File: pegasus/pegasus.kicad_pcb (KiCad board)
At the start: 2 copper layers, 50 x 120 mm, 15 parts, among them IC1 RFD900, IC2 Adafruit_MPL3115A2, IC3 Adafruit-BNO055-PCB, IC4 L70B-M39, IC5 L7805ACV, J1 Conn_01x02_Female, J2 Conn_01x02_Female, U1 Teensy4.1, U2 CON-SMA-EDGE-S, U3 CON-SMA-EDGE-S

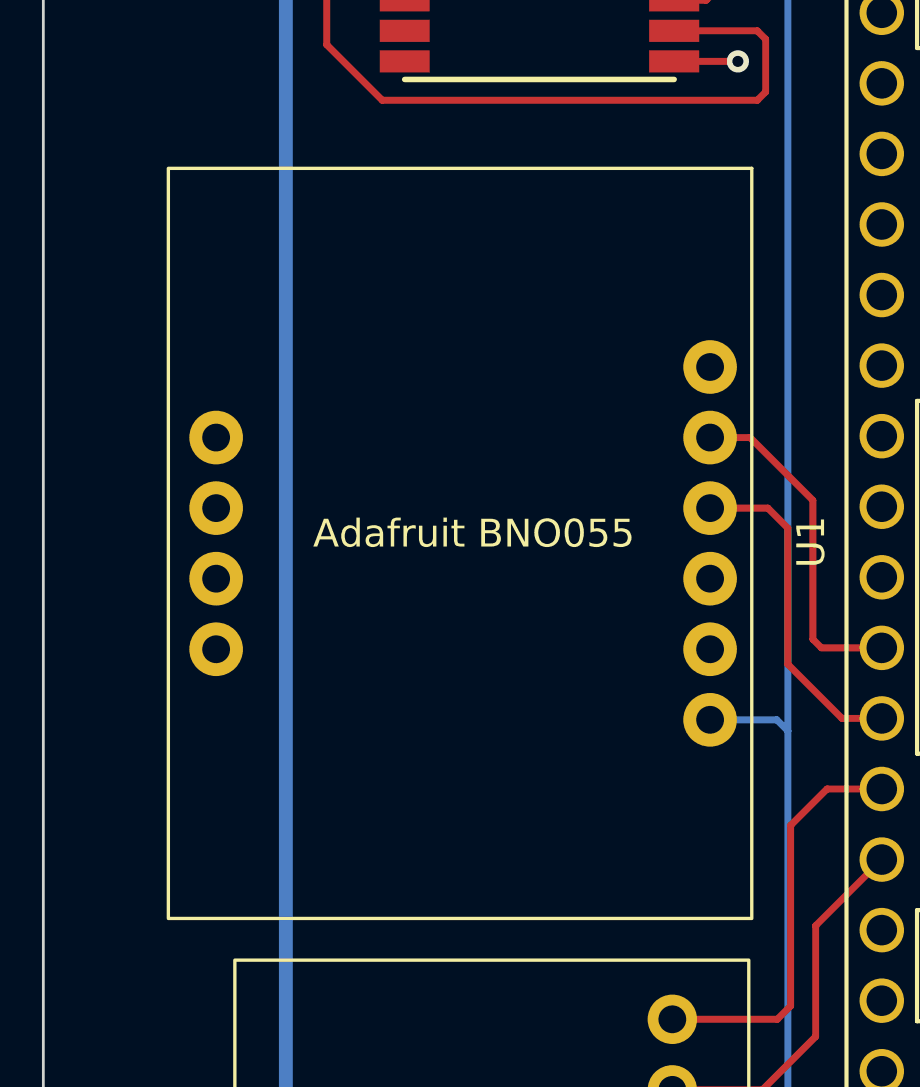
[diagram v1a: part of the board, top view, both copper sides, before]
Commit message: improved dimensional accuracy of Adafruit BNO055
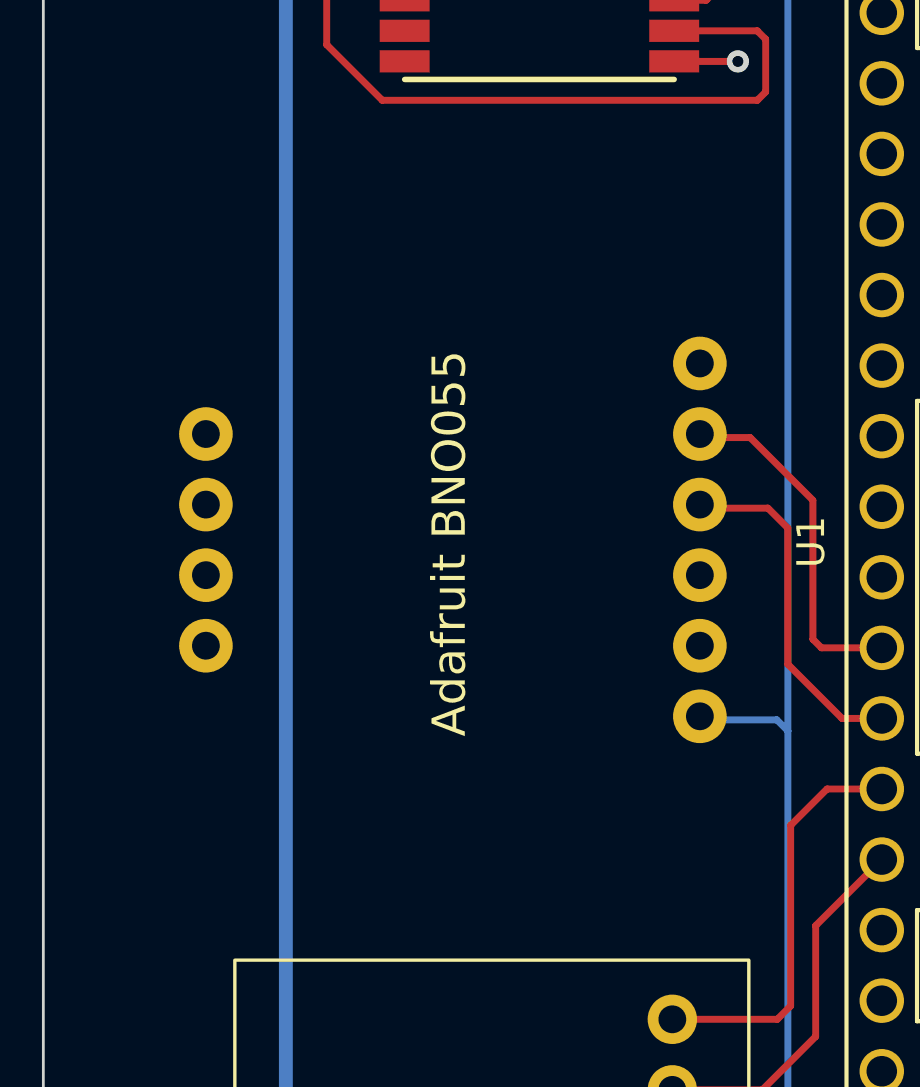
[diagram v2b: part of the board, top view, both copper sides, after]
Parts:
- IC3: footprint Adafruit_BNO055:adafruit_ -> Adafruit_BNO055:BNO055-B26.67x17.78mm-1x06_ROUND-1x04_ROUND-P2.54mm
- moved IC3 9.39 mm to (94.6, 115.3)
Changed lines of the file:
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@@
       (effects (font (size 1.27 1.27) (thickness 0.254)))
     )
+    (fp_line (start 7.75 -3.07) (end -2.65 -3.07) (layer "F.SilkS") (width 0.2))
+    (fp_line (start 7.75 1.53) (end 7.75 -3.07) (layer "F.SilkS") (width 0.2))
     (fp_line (start -2.65 -3.07) (end -2.65 0) (layer "F.SilkS") (width 0.2))
-    (fp_line (start 7.75 1.53) (end 7.75 -3.07) (layer "F.SilkS") (width 0.2))
-    (fp_line (start 7.75 -3.07) (end -2.65 -3.07) (layer "F.SilkS") (width 0.2))
     (fp_line (start -2.9 1.78) (end -2.9 -3.32) (layer "F.CrtYd") (width 0.05))
+    (fp_line (start -2.9 -3.32) (end 8 -3.32) (layer "F.CrtYd") (width 0.05))
+    (fp_line (start 8 -3.32) (end 8 1.78) (layer "F.CrtYd") (width 0.05))
     (fp_line (start 8 1.78) (end -2.9 1.78) (layer "F.CrtYd") (width 0.05))
-    (fp_line (start 8 -3.32) (end 8 1.78) (layer "F.CrtYd") (width 0.05))
-    (fp_line (start -2.9 -3.32) (end 8 -3.32) (layer "F.CrtYd") (width 0.05))
+    (fp_line (start -2.65 -3.07) (end 7.75 -3.07) (layer "F.Fab") (width 0.1))
     (fp_line (start -2.65 -1.795) (end -1.375 -3.07) (layer "F.Fab") (width 0.1))
     (fp_line (start 7.75 1.53) (end -2.65 1.53) (layer "F.Fab") (width 0.1))
     (fp_line (start 7.75 -3.07) (end 7.75 1.53) (layer "F.Fab") (width 0.1))
     (fp_line (start -2.65 1.53) (end -2.65 -3.07) (layer "F.Fab") (width 0.1))
-    (fp_line (start -2.65 -3.07) (end 7.75 -3.07) (layer "F.Fab") (width 0.1))
     (pad "1" thru_hole rect (at 0 0 180) (size 1.98 1.98) (drill 1.32) (layers *.Cu *.Mask)
       (net 106 "+3.7V") (pinfunction "INPUT") (pintype "passive"))
@@
     )
   )
-  (footprint "Adafruit_BNO055:adafruit_" (layer "F.Cu")
-    (at 104 115.35 90)
+  (footprint "Adafruit_BNO055:BNO055-B26.67x17.78mm-1x06_ROUND-1x04_ROUND-P2.54mm" (layer "F.Cu")
+    (at 94.615 115.35 90)
     (property "Sheetfile" "pegasus.kicad_sch")
     (property "Sheetname" "")
@@
       (effects (font (size 0.77216 0.77216) (thickness 0.146304)) (justify left bottom))
     )
-    (fp_text value "Adafruit-BNO055-PCB" (at -7.62 1.905 90) (layer "F.Fab")
-      (effects (font (size 0.38608 0.38608) (thickness 0.038608)) (justify left bottom))
-    )
-    (fp_text user "Adafruit BNO055" (at 0.35 -8.5 unlocked) (layer "F.SilkS")
-      (effects (font (size 1 1) (thickness 0.15)))
-    )
-    (fp_rect (start 13.5 1.5) (end -13.5 -19.5) (layer "F.SilkS") (width 0.12) (fill none))
-    (fp_line (start -7.62 -0.635) (end -7.62 0.635) (layer "F.Fab") (width 0.2032))
-    (fp_poly (pts
-        (xy 3.556 -17.526)
-        (xy 4.064 -17.526)
-        (xy 4.064 -18.034)
-        (xy 3.556 -18.034)
-      ) (layer "F.Fab") (width 0) (fill solid))
-    (fp_poly (pts
-        (xy 3.556 0.254)
-        (xy 4.064 0.254)
-        (xy 4.064 -0.254)
-        (xy 3.556 -0.254)
-      ) (layer "F.Fab") (width 0) (fill solid))
-    (fp_poly (pts
-        (xy -1.524 -17.526)
-        (xy -1.016 -17.526)
-        (xy -1.016 -18.034)
-        (xy -1.524 -18.034)
-      ) (layer "F.Fab") (width 0) (fill solid))
-    (fp_poly (pts
-        (xy 1.016 -17.526)
-        (xy 1.524 -17.526)
-        (xy 1.524 -18.034)
-        (xy 1.016 -18.034)
-      ) (layer "F.Fab") (width 0) (fill solid))
-    (fp_poly (pts
-        (xy -4.064 -17.526)
-        (xy -3.556 -17.526)
-        (xy -3.556 -18.034)
-        (xy -4.064 -18.034)
-      ) (layer "F.Fab") (width 0) (fill solid))
-    (fp_poly (pts
-        (xy -1.524 0.254)
-        (xy -1.016 0.254)
-        (xy -1.016 -0.254)
-        (xy -1.524 -0.254)
-      ) (layer "F.Fab") (width 0) (fill solid))
-    (fp_poly (pts
-        (xy -6.604 0.254)
-        (xy -6.096 0.254)
-        (xy -6.096 -0.254)
-        (xy -6.604 -0.254)
-      ) (layer "F.Fab") (width 0) (fill solid))
-    (fp_poly (pts
-        (xy -4.064 0.254)
-        (xy -3.556 0.254)
-        (xy -3.556 -0.254)
-        (xy -4.064 -0.254)
-      ) (layer "F.Fab") (width 0) (fill solid))
-    (fp_poly (pts
-        (xy 1.016 0.254)
-        (xy 1.524 0.254)
-        (xy 1.524 -0.254)
-        (xy 1.016 -0.254)
-      ) (layer "F.Fab") (width 0) (fill solid))
-    (fp_poly (pts
-        (xy 6.096 0.254)
-        (xy 6.604 0.254)
-        (xy 6.604 -0.254)
-        (xy 6.096 -0.254)
-      ) (layer "F.Fab") (width 0) (fill solid))
-    (pad "1" thru_hole circle (at -6.35 0 180) (size 1.9304 1.9304) (drill 1) (layers *.Cu *.Mask)
+    (fp_text value "Adafruit-BNO055-PCB" (at -23.368 -12.573 90) (layer "F.Fab")
+      (effects (font (size 1 1) (thickness 0.15)) (justify left bottom))
+    )
+    (fp_text user "Adafruit BNO055" (at 0 0 90 unlocked) (layer "F.SilkS")
+      (effects (font (size 1.2 1.2) (thickness 0.2)))
+    )
+    (fp_rect (start -13.458 -10.283) (end 13.708 10.533) (layer "F.CrtYd") (width 0.05) (fill none))
+    (fp_line (start -13.208 7.747) (end -13.208 -7.493) (layer "F.Fab") (width 0.1))
+    (fp_line (start 13.462 -7.493) (end 13.462 7.747) (layer "F.Fab") (width 0.1))
+    (fp_line (start 10.922 10.287) (end -10.668 10.287) (layer "F.Fab") (width 0.1))
+    (fp_line (start -4.953 -9.398) (end -4.953 -8.128) (layer "F.Fab") (width 0.2032))
+    (fp_line (start -10.668 -10.033) (end 10.922 -10.033) (layer "F.Fab") (width 0.1))
+    (fp_line (start -7.493 8.382) (end -7.493 9.652) (layer "F.Fab") (width 0.2032))
+    (fp_arc (start -13.208 -7.493) (mid -12.464051 -9.289051) (end -10.668 -10.033) (layer "F.Fab") (width 0.1))
+    (fp_arc (start 13.462 7.747) (mid 12.718051 9.543051) (end 10.922 10.287) (layer "F.Fab") (width 0.1))
+    (fp_arc (start -10.668 10.287) (mid -12.464051 9.543051) (end -13.208 7.747) (layer "F.Fab") (width 0.1))
+    (fp_arc (start 10.922 -10.033) (mid 12.718051 -9.289051) (end 13.462 -7.493) (layer "F.Fab") (width 0.1))
+    (pad "1" thru_hole circle (at -6.223 9.017 180) (size 1.9304 1.9304) (drill 1) (layers *.Cu *.Mask)
       (net 100 "/+3.3V") (pinfunction "Vin_5V") (pintype "bidirectional") (solder_mask_margin 0.0508))
-    (pad "2" thru_hole circle (at -3.81 0 180) (size 1.9304 1.9304) (drill 1) (layers *.Cu *.Mask)
+    (pad "2" thru_hole circle (at -3.683 9.017 180) (size 1.9304 1.9304) (drill 1) (layers *.Cu *.Mask)
       (net 34 "unconnected-(IC3-Pad2)") (pinfunction "3.3Vo") (pintype "bidirectional+no_connect") (solder_mask_margin 0.0508))
-    (pad "3" thru_hole circle (at -1.27 0 180) (size 1.9304 1.9304) (drill 1) (layers *.Cu *.Mask)
+    (pad "3" thru_hole circle (at -1.143 9.017 180) (size 1.9304 1.9304) (drill 1) (layers *.Cu *.Mask)
       (net 2 "GND") (pinfunction "GND") (pintype "bidirectional") (solder_mask_margin 0.0508))
-    (pad "4" thru_hole circle (at 1.27 0 180) (size 1.9304 1.9304) (drill 1) (layers *.Cu *.Mask)
+    (pad "4" thru_hole circle (at 1.397 9.017 180) (size 1.9304 1.9304) (drill 1) (layers *.Cu *.Mask)
       (net 103 "/SDA1") (pinfunction "SDA_5V") (pintype "bidirectional") (solder_mask_margin 0.0508))
-    (pad "5" thru_hole circle (at 3.81 0 180) (size 1.9304 1.9304) (drill 1) (layers *.Cu *.Mask)
+    (pad "5" thru_hole circle (at 3.937 9.017 180) (size 1.9304 1.9304) (drill 1) (layers *.Cu *.Mask)
       (net 104 "/SCL1") (pinfunction "SCL-5V") (pintype "bidirectional") (solder_mask_margin 0.0508))
-    (pad "6" thru_hole circle (at 6.35 0 180) (size 1.9304 1.9304) (drill 1) (layers *.Cu *.Mask)
+    (pad "6" thru_hole circle (at 6.477 9.017 180) (size 1.9304 1.9304) (drill 1) (layers *.Cu *.Mask)
       (net 16 "unconnected-(IC3-Pad6)") (pinfunction "RST_5V") (pintype "bidirectional+no_connect") (solder_mask_margin 0.0508))
-    (pad "7" thru_hole circle (at -3.81 -17.78 180) (size 1.9304 1.9304) (drill 1) (layers *.Cu *.Mask)
+    (pad "7" thru_hole circle (at -3.683 -8.763 180) (size 1.9304 1.9304) (drill 1) (layers *.Cu *.Mask)
       (net 17 "unconnected-(IC3-Pad7)") (pinfunction "PS0_3V") (pintype "bidirectional+no_connect") (solder_mask_margin 0.0508))
-    (pad "8" thru_hole circle (at -1.27 -17.78 180) (size 1.9304 1.9304) (drill 1) (layers *.Cu *.Mask)
+    (pad "8" thru_hole circle (at -1.143 -8.763 180) (size 1.9304 1.9304) (drill 1) (layers *.Cu *.Mask)
       (net 107 "unconnected-(IC3-Pad8)") (pinfunction "PS1_3V") (pintype "bidirectional+no_connect") (solder_mask_margin 0.0508))
-    (pad "9" thru_hole circle (at 1.27 -17.78 180) (size 1.9304 1.9304) (drill 1) (layers *.Cu *.Mask)
+    (pad "9" thru_hole circle (at 1.397 -8.763 180) (size 1.9304 1.9304) (drill 1) (layers *.Cu *.Mask)
       (net 108 "unconnected-(IC3-Pad9)") (pinfunction "INT_3V") (pintype "bidirectional+no_connect") (solder_mask_margin 0.0508))
-    (pad "10" thru_hole circle (at 3.81 -17.78 180) (size 1.9304 1.9304) (drill 1) (layers *.Cu *.Mask)
+    (pad "10" thru_hole circle (at 3.937 -8.763 180) (size 1.9304 1.9304) (drill 1) (layers *.Cu *.Mask)
       (net 109 "unconnected-(IC3-Pad10)") (pinfunction "I2CAddr_3V") (pintype "bidirectional+no_connect") (solder_mask_margin 0.0508))
   )
